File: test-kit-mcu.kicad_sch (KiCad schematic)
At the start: 1 part, among them J1 DIN41612_02x32_AB

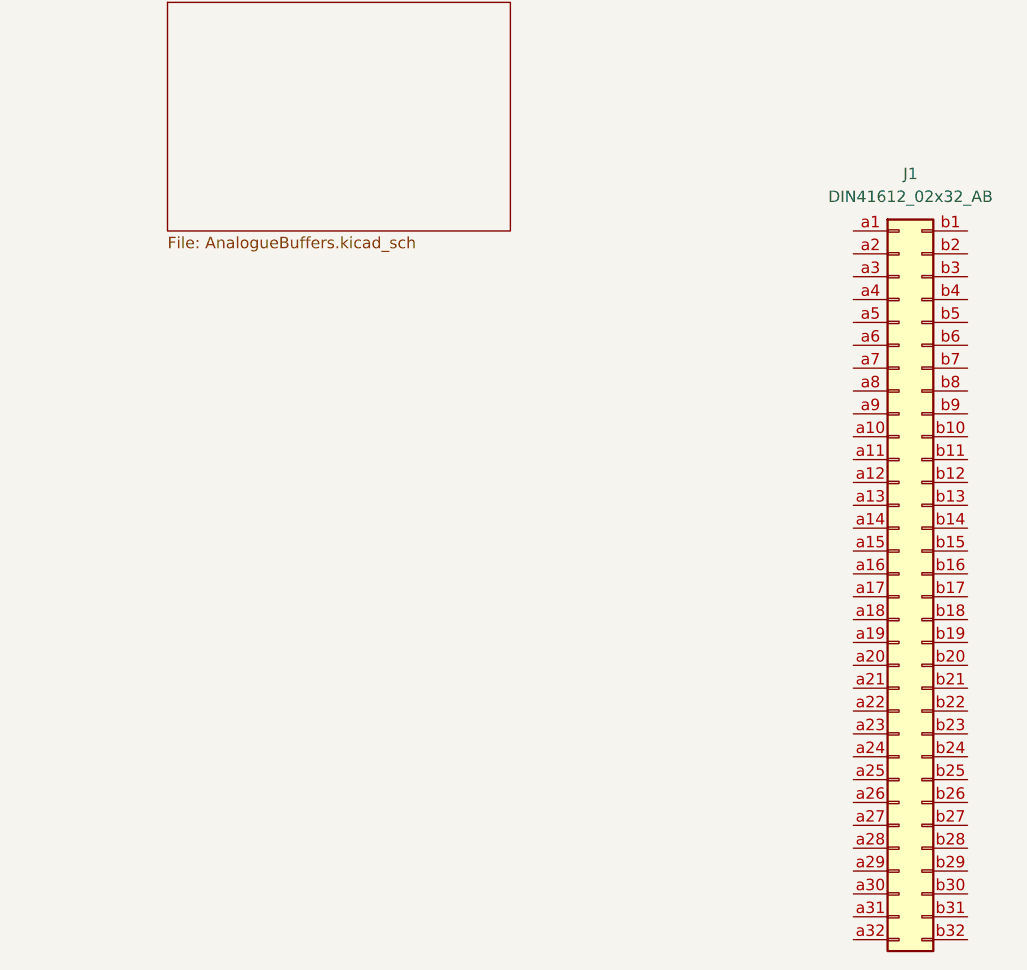
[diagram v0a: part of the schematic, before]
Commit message: Fleshed out digital IO
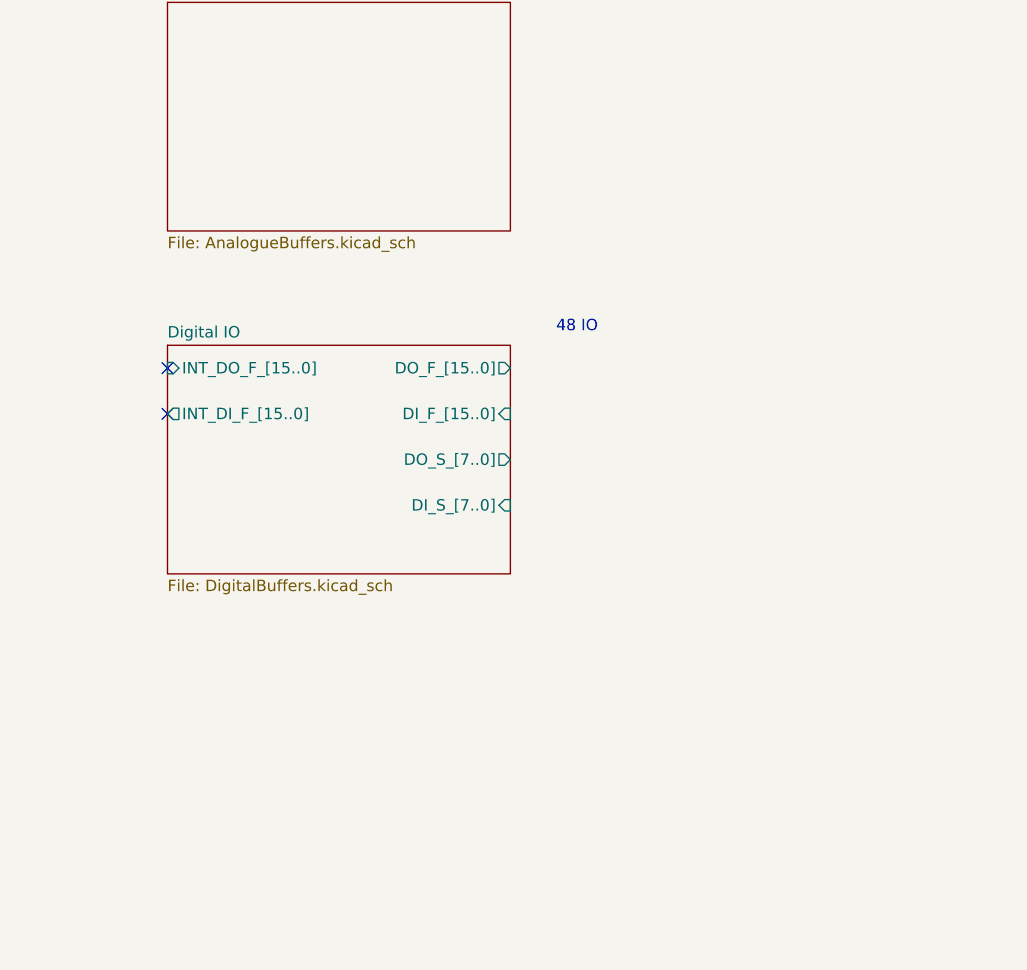
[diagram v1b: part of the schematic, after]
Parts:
- removed J1: DIN41612_02x32_AB, Connector_DIN:DIN41612_B_2x32_Female_Vertical_THT, symbol Connector:DIN41612_02x32_AB
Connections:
- no-connect marks 0 -> 2
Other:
- added sheet Digital IO (DigitalBuffers.kicad_sch)
- note added: "48 IO"

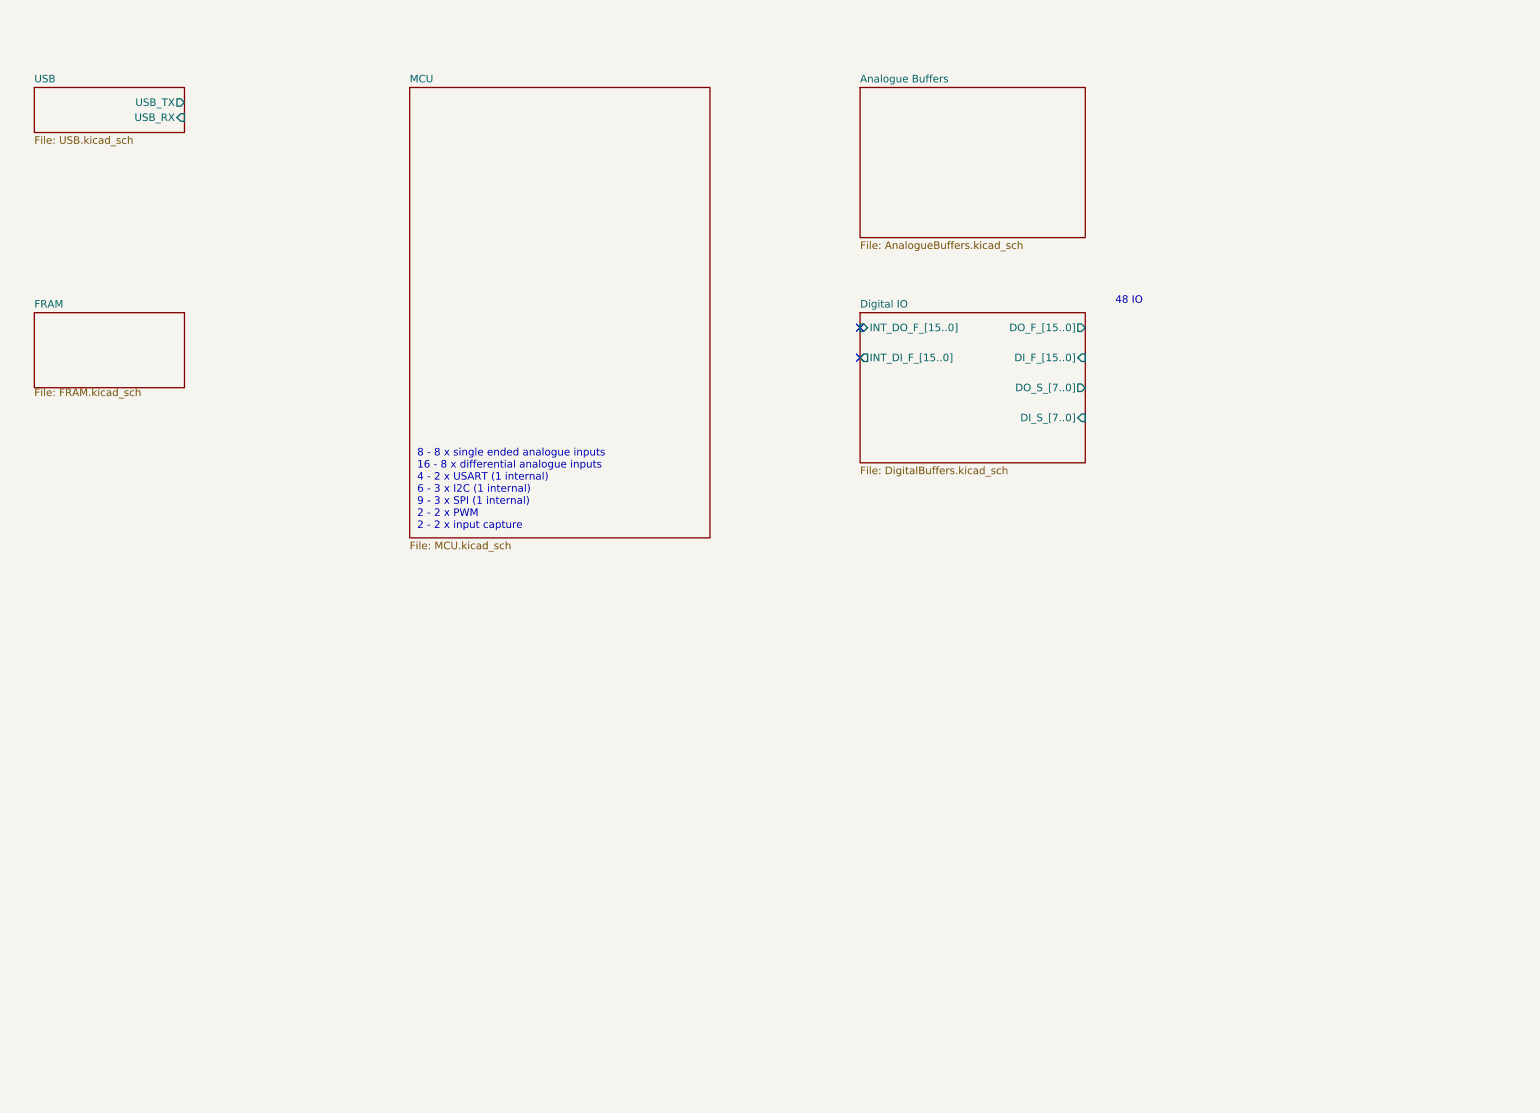
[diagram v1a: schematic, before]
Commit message: analog inputs, timer IO
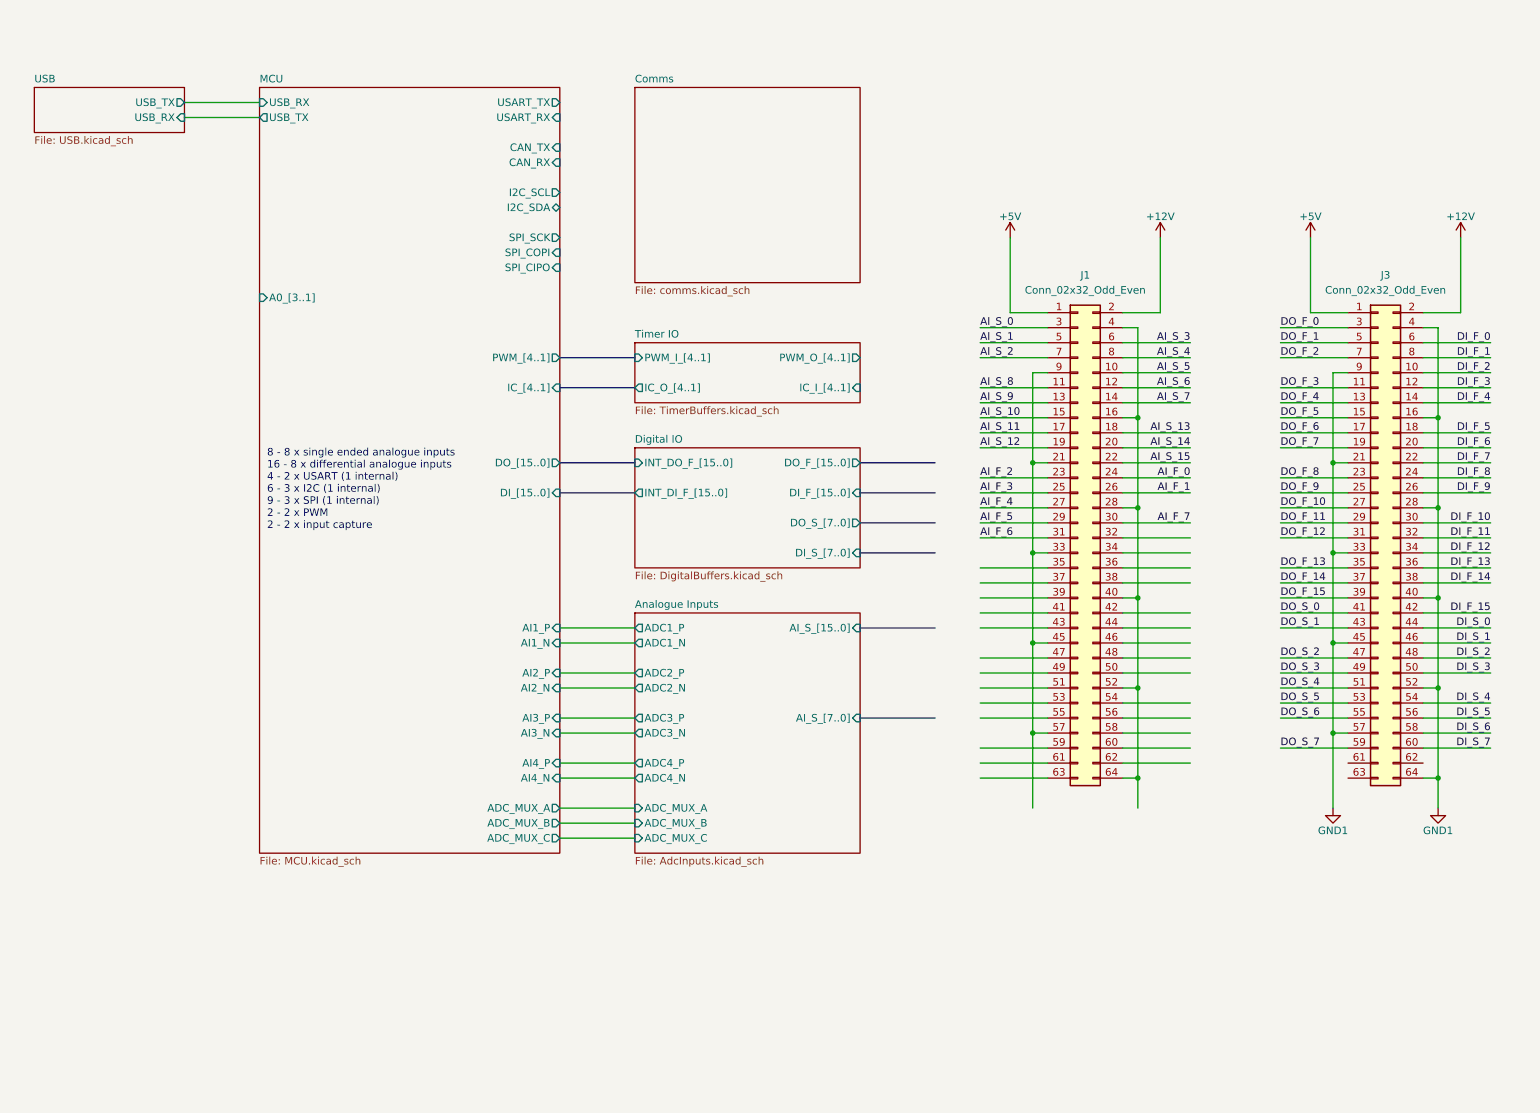
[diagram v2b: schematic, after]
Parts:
- added J1, J3: Conn_02x32_Odd_Even, Connector_PinHeader_2.00mm:PinHeader_2x32_P2.00mm_Vertical, symbol Connector_Generic:Conn_02x32_Odd_Even
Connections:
- new net: J1.16 (Pin_16), J1.28 (Pin_28), J1.4 (Pin_4), J1.40 (Pin_40), J1.52 (Pin_52), J1.64 (Pin_64)
- new net: J1.21 (Pin_21), J1.33 (Pin_33), J1.45 (Pin_45), J1.57 (Pin_57), J1.9 (Pin_9)
- new net +12V: J1.2 (Pin_2), J3.2 (Pin_2)
- new net +5V: J1.1 (Pin_1), J3.1 (Pin_1)
- new net AI_F_0: J1.24 (Pin_24)
- new net AI_F_1: J1.26 (Pin_26)
- new net AI_F_2: J1.23 (Pin_23)
- new net AI_F_3: J1.25 (Pin_25)
- new net AI_F_4: J1.27 (Pin_27)
- new net AI_F_5: J1.29 (Pin_29)
- new net AI_F_6: J1.31 (Pin_31)
- new net AI_F_7: J1.30 (Pin_30)
- new net AI_S_0: J1.3 (Pin_3)
- new net AI_S_1: J1.5 (Pin_5)
- new net AI_S_10: J1.15 (Pin_15)
- new net AI_S_11: J1.17 (Pin_17)
- new net AI_S_12: J1.19 (Pin_19)
- new net AI_S_13: J1.18 (Pin_18)
- new net AI_S_14: J1.20 (Pin_20)
- new net AI_S_15: J1.22 (Pin_22)
- new net AI_S_2: J1.7 (Pin_7)
- new net AI_S_3: J1.6 (Pin_6)
- new net AI_S_4: J1.8 (Pin_8)
- new net AI_S_5: J1.10 (Pin_10)
- new net AI_S_6: J1.12 (Pin_12)
- new net AI_S_7: J1.14 (Pin_14)
- new net AI_S_8: J1.11 (Pin_11)
- new net AI_S_9: J1.13 (Pin_13)
- new net DI_F_0: J3.6 (Pin_6)
- new net DI_F_1: J3.8 (Pin_8)
- new net DI_F_10: J3.30 (Pin_30)
- new net DI_F_11: J3.32 (Pin_32)
- new net DI_F_12: J3.34 (Pin_34)
- new net DI_F_13: J3.36 (Pin_36)
- new net DI_F_14: J3.38 (Pin_38)
- new net DI_F_15: J3.42 (Pin_42)
- new net DI_F_2: J3.10 (Pin_10)
- new net DI_F_3: J3.12 (Pin_12)
- new net DI_F_4: J3.14 (Pin_14)
- new net DI_F_5: J3.18 (Pin_18)
- new net DI_F_6: J3.20 (Pin_20)
- new net DI_F_7: J3.22 (Pin_22)
- new net DI_F_8: J3.24 (Pin_24)
- new net DI_F_9: J3.26 (Pin_26)
- new net DI_S_0: J3.44 (Pin_44)
- new net DI_S_1: J3.46 (Pin_46)
- new net DI_S_2: J3.48 (Pin_48)
- new net DI_S_3: J3.50 (Pin_50)
- new net DI_S_4: J3.54 (Pin_54)
- new net DI_S_5: J3.56 (Pin_56)
- new net DI_S_6: J3.58 (Pin_58)
- new net DI_S_7: J3.60 (Pin_60)
- new net DO_F_0: J3.3 (Pin_3)
- new net DO_F_1: J3.5 (Pin_5)
- new net DO_F_10: J3.27 (Pin_27)
- new net DO_F_11: J3.29 (Pin_29)
- new net DO_F_12: J3.31 (Pin_31)
- new net DO_F_13: J3.35 (Pin_35)
- new net DO_F_14: J3.37 (Pin_37)
- new net DO_F_15: J3.39 (Pin_39)
- new net DO_F_2: J3.7 (Pin_7)
- new net DO_F_3: J3.11 (Pin_11)
- new net DO_F_4: J3.13 (Pin_13)
- new net DO_F_5: J3.15 (Pin_15)
- new net DO_F_6: J3.17 (Pin_17)
- new net DO_F_7: J3.19 (Pin_19)
- new net DO_F_8: J3.23 (Pin_23)
- new net DO_F_9: J3.25 (Pin_25)
- new net DO_S_0: J3.41 (Pin_41)
- new net DO_S_1: J3.43 (Pin_43)
- new net DO_S_2: J3.47 (Pin_47)
- new net DO_S_3: J3.49 (Pin_49)
- new net DO_S_4: J3.51 (Pin_51)
- new net DO_S_5: J3.53 (Pin_53)
- new net DO_S_6: J3.55 (Pin_55)
- new net DO_S_7: J3.59 (Pin_59)
- new net GND1: J3.16 (Pin_16), J3.21 (Pin_21), J3.28 (Pin_28), J3.33 (Pin_33), J3.4 (Pin_4), J3.40 (Pin_40), J3.45 (Pin_45), J3.52 (Pin_52), J3.57 (Pin_57), J3.64 (Pin_64), J3.9 (Pin_9)
- no-connect marks 2 -> 0
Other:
- sheet Analogue Buffers renamed Analogue Inputs
- removed sheet FRAM
- added sheet Comms (comms.kicad_sch)
- added sheet Timer IO (TimerBuffers.kicad_sch)
- sheet Analogue Inputs: file AnalogueBuffers.kicad_sch -> AdcInputs.kicad_sch
- sheet Analogue Inputs ports: added ADC1_N, ADC1_P, ADC2_N, ADC2_P, ADC3_N, ADC3_P, ADC4_N, ADC4_P, ADC_MUX_A, ADC_MUX_B, ADC_MUX_C, AI_S_[15..0], AI_S_[7..0]; removed none
- sheet MCU ports: added A0_[3..1], ADC_MUX_A, ADC_MUX_B, ADC_MUX_C, AI1_N, AI1_P, AI2_N, AI2_P, AI3_N, AI3_P, AI4_N, AI4_P, CAN_RX, CAN_TX, DI_[15..0], DO_[15..0], I2C_SCL, I2C_SDA, IC_[4..1], PWM_[4..1], SPI_CIPO, SPI_COPI, SPI_SCK, USART_RX, USART_TX, USB_RX, USB_TX; removed none
- note removed: "48 IO"

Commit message: first draft schematic?
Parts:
- removed J1, J3: Conn_02x32_Odd_Even, Connector_PinHeader_2.00mm:PinHeader_2x32_P2.00mm_Vertical, symbol Connector_Generic:Conn_02x32_Odd_Even
- added J1, J3, J4, J5: Conn_02x16_Odd_Even, Connector_PinHeader_2.00mm:PinHeader_2x32_P2.00mm_Horizontal, symbol Connector_Generic:Conn_02x16_Odd_Even
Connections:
- net +12V: now also J1.2 (Pin_2), J3.2 (Pin_2), J4.2 (Pin_2), J5.2 (Pin_2)
- net +5V: now also J1.1 (Pin_1), J3.1 (Pin_1), J4.1 (Pin_1), J5.1 (Pin_1)
- net AI_F_0: now also J1.23 (Pin_23)
- net AI_F_1: now also J1.25 (Pin_25)
- net AI_F_2: now also J1.27 (Pin_27)
- net AI_F_3: now also J1.29 (Pin_29)
- net AI_F_4: now also J1.24 (Pin_24)
- net AI_F_5: now also J1.26 (Pin_26)
- net AI_F_6: now also J1.30 (Pin_30)
- net AI_F_7: now also J1.32 (Pin_32)
- net AI_S_0: now also J1.3 (Pin_3)
- net AI_S_1: now also J1.5 (Pin_5)
- net AI_S_10: now also J1.10 (Pin_10)
- net AI_S_11: now also J1.12 (Pin_12)
- net AI_S_12: now also J1.14 (Pin_14)
- net AI_S_13: now also J1.18 (Pin_18)
- net AI_S_14: now also J1.20 (Pin_20)
- net AI_S_15: now also J1.22 (Pin_22)
- net AI_S_2: now also J1.7 (Pin_7)
- net AI_S_3: now also J1.11 (Pin_11)
- net AI_S_4: now also J1.13 (Pin_13)
- net AI_S_5: now also J1.15 (Pin_15)
- net AI_S_6: now also J1.17 (Pin_17)
- net AI_S_7: now also J1.19 (Pin_19)
- net AI_S_8: now also J1.6 (Pin_6)
- net AI_S_9: now also J1.8 (Pin_8)
- net DI_F_0: now also J4.3 (Pin_3)
- net DI_F_1: now also J4.5 (Pin_5)
- net DI_F_10: now also J4.10 (Pin_10)
- net DI_F_11: now also J4.12 (Pin_12)
- net DI_F_12: now also J4.14 (Pin_14)
- net DI_F_13: now also J4.18 (Pin_18)
- net DI_F_14: now also J4.20 (Pin_20)
- net DI_F_15: now also J4.22 (Pin_22)
- net DI_F_2: now also J4.7 (Pin_7)
- net DI_F_3: now also J4.11 (Pin_11)
- net DI_F_4: now also J4.13 (Pin_13)
- net DI_F_5: now also J4.15 (Pin_15)
- net DI_F_6: now also J4.17 (Pin_17)
- net DI_F_7: now also J4.19 (Pin_19)
- net DI_F_8: now also J4.6 (Pin_6)
- net DI_F_9: now also J4.8 (Pin_8)
- net DI_S_0: now also J4.23 (Pin_23)
- net DI_S_1: now also J4.25 (Pin_25)
- net DI_S_2: now also J4.27 (Pin_27)
- net DI_S_3: now also J4.29 (Pin_29)
- net DI_S_4: now also J4.24 (Pin_24)
- net DI_S_5: now also J4.26 (Pin_26)
- net DI_S_6: now also J4.30 (Pin_30)
- net DI_S_7: now also J4.32 (Pin_32)
- net DO_F_0: now also J5.3 (Pin_3)
- net DO_F_1: now also J5.5 (Pin_5)
- net DO_F_10: now also J5.10 (Pin_10)
- net DO_F_11: now also J5.12 (Pin_12)
- net DO_F_12: now also J5.14 (Pin_14)
- net DO_F_13: now also J5.18 (Pin_18)
- net DO_F_14: now also J5.20 (Pin_20)
- net DO_F_15: now also J5.22 (Pin_22)
- net DO_F_2: now also J5.7 (Pin_7)
- net DO_F_3: now also J5.11 (Pin_11)
- net DO_F_4: now also J5.13 (Pin_13)
- net DO_F_5: now also J5.15 (Pin_15)
- net DO_F_6: now also J5.17 (Pin_17)
- net DO_F_7: now also J5.19 (Pin_19)
- net DO_F_8: now also J5.6 (Pin_6)
- net DO_F_9: now also J5.8 (Pin_8)
- net DO_S_0: now also J5.23 (Pin_23)
- net DO_S_1: now also J5.25 (Pin_25)
- net DO_S_2: now also J5.27 (Pin_27)
- net DO_S_3: now also J5.29 (Pin_29)
- net DO_S_4: now also J5.24 (Pin_24)
- net DO_S_5: now also J5.26 (Pin_26)
- net DO_S_6: now also J5.30 (Pin_30)
- net DO_S_7: now also J5.32 (Pin_32)
- net GND1: now also J1.16 (Pin_16), J1.21 (Pin_21), J1.28 (Pin_28), J1.31 (Pin_31), J1.4 (Pin_4), J1.9 (Pin_9), J3.16 (Pin_16), J3.21 (Pin_21), J3.28 (Pin_28), J3.31 (Pin_31), J3.4 (Pin_4), J3.9 (Pin_9), J4.16 (Pin_16), J4.21 (Pin_21), J4.28 (Pin_28), J4.31 (Pin_31), J4.4 (Pin_4), J4.9 (Pin_9), J5.16 (Pin_16), J5.21 (Pin_21), J5.28 (Pin_28), J5.31 (Pin_31), J5.4 (Pin_4), J5.9 (Pin_9)
- new net IC_1: J3.6 (Pin_6)
- new net IC_2: J3.8 (Pin_8)
- new net IC_3: J3.10 (Pin_10)
- new net IC_4: J3.12 (Pin_12)
- new net PWM_1: J3.3 (Pin_3)
- new net PWM_2: J3.5 (Pin_5)
- new net PWM_3: J3.7 (Pin_7)
- new net PWM_4: J3.11 (Pin_11)
- new net PWM_5: J3.13 (Pin_13)
- new net PWM_6: J3.15 (Pin_15)
- new net PWM_7: J3.17 (Pin_17)
- new net UUT_CAN_H: J3.24 (Pin_24)
- new net UUT_CAN_L: J3.26 (Pin_26)
- new net UUT_I2C_SCL: J3.25 (Pin_25)
- new net UUT_I2C_SDA: J3.27 (Pin_27)
- new net UUT_SPI_CIPO: J3.32 (Pin_32)
- new net UUT_SPI_COPI: J3.30 (Pin_30)
- new net UUT_SPI_SCK: J3.29 (Pin_29)
- new net UUT_USART_RX: J3.22 (Pin_22)
- new net UUT_USART_TX: J3.23 (Pin_23)
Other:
- sheet Analogue Inputs ports: added AI_F_[7..0]; removed AI_S_[7..0]
- sheet Comms ports: added CAN_RX, CAN_TX, I2C_SCL, I2C_SDA, SPI_CIPO, SPI_COPI, SPI_SCK, USART_MCU_RX, USART_MCU_TX, UUT_CAN_H, UUT_CAN_L, UUT_CIPO, UUT_COPI, UUT_I2C_SCL, UUT_I2C_SDA, UUT_SCK, UUT_USART_RX, UUT_USART_TX; removed none
- sheet MCU ports: added PWM_[8..1]; removed PWM_[4..1]
- sheet Timer IO ports: added PWM_I_[8..1], PWM_O_[8..1]; removed PWM_I_[4..1], PWM_O_[4..1]
- title: (none) -> STM23G4 MCU TEST KIT
